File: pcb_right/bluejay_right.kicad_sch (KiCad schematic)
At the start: 69 parts, among them J2 SJ-43514, U2 MCP23017

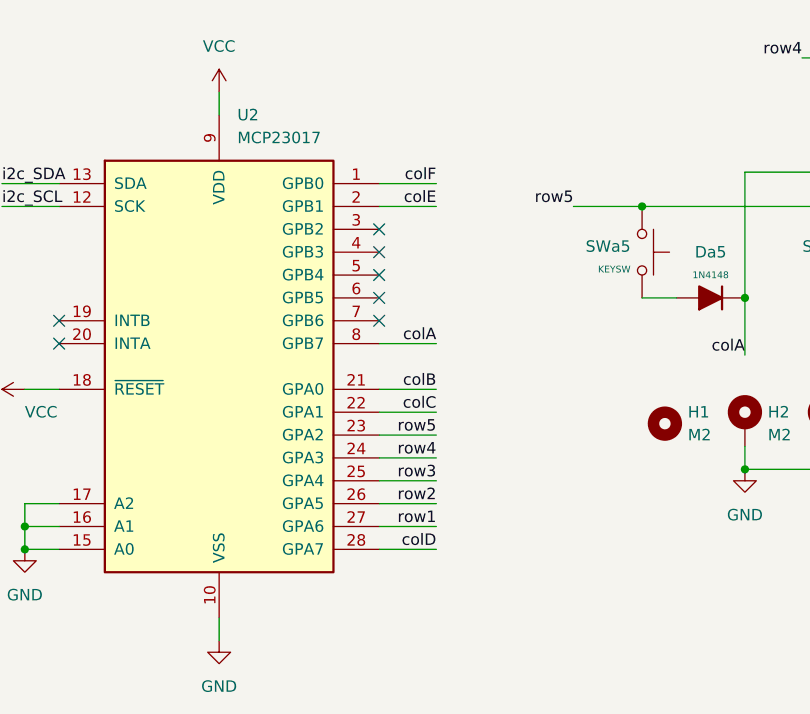
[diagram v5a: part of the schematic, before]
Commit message: Create base pcb
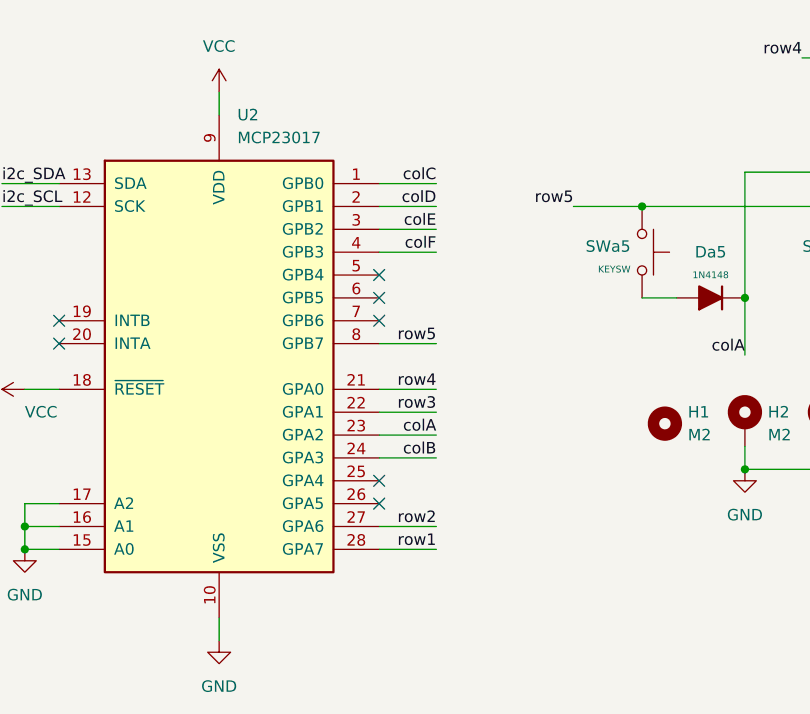
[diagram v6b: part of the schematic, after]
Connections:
- net colA: now also U2.23 (GPA2); no longer U2.8 (GPB7)
- net colB: now also U2.24 (GPA3); no longer U2.21 (GPA0)
- net colC: now also U2.1 (GPB0); no longer U2.22 (GPA1)
- net colD: now also U2.2 (GPB1); no longer U2.28 (GPA7)
- net colE: now also U2.3 (GPB2); no longer U2.2 (GPB1)
- net colF: now also U2.4 (GPB3); no longer U2.1 (GPB0)
- net row1: now also U2.28 (GPA7); no longer U2.27 (GPA6)
- net row2: now also U2.27 (GPA6); no longer U2.26 (GPA5)
- net row3: now also U2.22 (GPA1); no longer U2.25 (GPA4)
- net row4: now also U2.21 (GPA0); no longer U2.24 (GPA3)
- net row5: now also U2.8 (GPB7); no longer U2.23 (GPA2)
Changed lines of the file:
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@@
   (junction (at 104.14 120.65) (diameter 0) (color 0 0 0 0)
   )
-  (no_connect (at 63.5 101.6))
-  (no_connect (at 63.5 96.52))
   (no_connect (at 63.5 99.06))
   (no_connect (at 63.5 104.14))
-  (no_connect (at 63.5 93.98))
+  (no_connect (at 63.5 101.6))
   (no_connect (at 27.94 104.14))
   (no_connect (at 27.94 106.68))
+  (no_connect (at 63.5 124.46))
+  (no_connect (at 63.5 121.92))
   (wire (pts (xy 55.88 49.53) (xy 55.88 52.07))
     (stroke (width 0) (type default) (color 0 0 0 0))
   )
+  (wire (pts (xy 48.26 49.53) (xy 48.26 59.69))
+    (stroke (width 0) (type default) (color 0 0 0 0))
+  )
+  (wire (pts (xy 222.25 59.69) (xy 218.44 59.69))
+    (stroke (width 0) (type default) (color 0 0 0 0))
+  )
+  (wire (pts (xy 133.35 59.69) (xy 133.35 72.39))
+    (stroke (width 0) (type default) (color 0 0 0 0))
+  )
+  (wire (pts (xy 194.31 36.83) (xy 170.18 36.83))
+    (stroke (width 0) (type default) (color 0 0 0 0))
+  )
+  (wire (pts (xy 246.38 72.39) (xy 242.57 72.39))
+    (stroke (width 0) (type default) (color 0 0 0 0))
+  )
+  (wire (pts (xy 63.5 119.38) (xy 69.85 119.38))
+    (stroke (width 0) (type default) (color 0 0 0 0))
+  )
+  (wire (pts (xy 48.26 59.69) (xy 58.42 59.69))
+    (stroke (width 0) (type default) (color 0 0 0 0))
+  )
+  (wire (pts (xy 246.38 85.09) (xy 242.57 85.09))
+    (stroke (width 0) (type default) (color 0 0 0 0))
+  )
+  (wire (pts (xy 181.61 85.09) (xy 181.61 90.17))
+    (stroke (width 0) (type default) (color 0 0 0 0))
+  )
+  (wire (pts (xy 219.71 104.14) (xy 219.71 105.41))
+    (stroke (width 0) (type default) (color 0 0 0 0))
+  )
+  (wire (pts (xy 113.03 118.11) (xy 113.03 120.65))
+    (stroke (width 0) (type default) (color 0 0 0 0))
+  )
+  (wire (pts (xy 152.4 90.17) (xy 152.4 101.6))
+    (stroke (width 0) (type default) (color 0 0 0 0))
+  )
+  (wire (pts (xy 104.14 87.63) (xy 104.14 101.6))
+    (stroke (width 0) (type default) (color 0 0 0 0))
+  )
+  (wire (pts (xy 48.26 40.64) (xy 48.26 44.45))
+    (stroke (width 0) (type default) (color 0 0 0 0))
+  )
+  (wire (pts (xy 246.38 59.69) (xy 242.57 59.69))
+    (stroke (width 0) (type default) (color 0 0 0 0))
+  )
+  (wire (pts (xy 198.12 59.69) (xy 194.31 59.69))
+    (stroke (width 0) (type default) (color 0 0 0 0))
+  )
+  (wire (pts (xy 121.92 49.53) (xy 110.49 49.53))
+    (stroke (width 0) (type default) (color 0 0 0 0))
+  )
+  (wire (pts (xy 194.31 74.93) (xy 170.18 74.93))
+    (stroke (width 0) (type default) (color 0 0 0 0))
+  )
+  (wire (pts (xy 38.1 52.07) (xy 55.88 52.07))
+    (stroke (width 0) (type default) (color 0 0 0 0))
+  )
+  (wire (pts (xy 173.99 46.99) (xy 170.18 46.99))
+    (stroke (width 0) (type default) (color 0 0 0 0))
+  )
+  (wire (pts (xy 125.73 85.09) (xy 121.92 85.09))
+    (stroke (width 0) (type default) (color 0 0 0 0))
+  )
+  (wire (pts (xy 21.59 88.9) (xy 27.94 88.9))
+    (stroke (width 0) (type default) (color 0 0 0 0))
+  )
+  (wire (pts (xy 205.74 72.39) (xy 205.74 85.09))
+    (stroke (width 0) (type default) (color 0 0 0 0))
+  )
   (wire (pts (xy 63.5 116.84) (xy 69.85 116.84))
     (stroke (width 0) (type default) (color 0 0 0 0))
   )
-  (wire (pts (xy 48.26 49.53) (xy 48.26 59.69))
-    (stroke (width 0) (type default) (color 0 0 0 0))
-  )
-  (wire (pts (xy 222.25 59.69) (xy 218.44 59.69))
-    (stroke (width 0) (type default) (color 0 0 0 0))
-  )
-  (wire (pts (xy 133.35 59.69) (xy 133.35 72.39))
-    (stroke (width 0) (type default) (color 0 0 0 0))
-  )
-  (wire (pts (xy 194.31 36.83) (xy 170.18 36.83))
-    (stroke (width 0) (type default) (color 0 0 0 0))
-  )
-  (wire (pts (xy 63.5 121.92) (xy 69.85 121.92))
-    (stroke (width 0) (type default) (color 0 0 0 0))
-  )
-  (wire (pts (xy 246.38 72.39) (xy 242.57 72.39))
-    (stroke (width 0) (type default) (color 0 0 0 0))
-  )
-  (wire (pts (xy 48.26 59.69) (xy 58.42 59.69))
-    (stroke (width 0) (type default) (color 0 0 0 0))
-  )
-  (wire (pts (xy 246.38 85.09) (xy 242.57 85.09))
-    (stroke (width 0) (type default) (color 0 0 0 0))
-  )
-  (wire (pts (xy 181.61 85.09) (xy 181.61 90.17))
-    (stroke (width 0) (type default) (color 0 0 0 0))
-  )
-  (wire (pts (xy 219.71 104.14) (xy 219.71 105.41))
-    (stroke (width 0) (type default) (color 0 0 0 0))
-  )
-  (wire (pts (xy 113.03 118.11) (xy 113.03 120.65))
-    (stroke (width 0) (type default) (color 0 0 0 0))
-  )
-  (wire (pts (xy 152.4 90.17) (xy 152.4 101.6))
-    (stroke (width 0) (type default) (color 0 0 0 0))
-  )
-  (wire (pts (xy 104.14 87.63) (xy 104.14 101.6))
-    (stroke (width 0) (type default) (color 0 0 0 0))
-  )
-  (wire (pts (xy 48.26 40.64) (xy 48.26 44.45))
-    (stroke (width 0) (type default) (color 0 0 0 0))
-  )
-  (wire (pts (xy 246.38 59.69) (xy 242.57 59.69))
-    (stroke (width 0) (type default) (color 0 0 0 0))
-  )
-  (wire (pts (xy 198.12 59.69) (xy 194.31 59.69))
-    (stroke (width 0) (type default) (color 0 0 0 0))
-  )
-  (wire (pts (xy 121.92 49.53) (xy 110.49 49.53))
-    (stroke (width 0) (type default) (color 0 0 0 0))
-  )
-  (wire (pts (xy 194.31 74.93) (xy 170.18 74.93))
-    (stroke (width 0) (type default) (color 0 0 0 0))
-  )
-  (wire (pts (xy 38.1 52.07) (xy 55.88 52.07))
-    (stroke (width 0) (type default) (color 0 0 0 0))
-  )
-  (wire (pts (xy 173.99 46.99) (xy 170.18 46.99))
-    (stroke (width 0) (type default) (color 0 0 0 0))
-  )
-  (wire (pts (xy 125.73 85.09) (xy 121.92 85.09))
-    (stroke (width 0) (type default) (color 0 0 0 0))
-  )
-  (wire (pts (xy 21.59 88.9) (xy 27.94 88.9))
-    (stroke (width 0) (type default) (color 0 0 0 0))
-  )
-  (wire (pts (xy 205.74 72.39) (xy 205.74 85.09))
-    (stroke (width 0) (type default) (color 0 0 0 0))
-  )
   (wire (pts (xy 21.59 91.44) (xy 27.94 91.44))
     (stroke (width 0) (type default) (color 0 0 0 0))
@@
     (stroke (width 0) (type default) (color 0 0 0 0))
   )
-  (wire (pts (xy 63.5 119.38) (xy 69.85 119.38))
-    (stroke (width 0) (type default) (color 0 0 0 0))
-  )
   (wire (pts (xy 133.35 72.39) (xy 133.35 85.09))
     (stroke (width 0) (type default) (color 0 0 0 0))
@@
     (stroke (width 0) (type default) (color 0 0 0 0))
   )
-  (wire (pts (xy 63.5 124.46) (xy 69.85 124.46))
-    (stroke (width 0) (type default) (color 0 0 0 0))
-  )
   (wire (pts (xy 152.4 101.6) (xy 152.4 107.95))
     (stroke (width 0) (type default) (color 0 0 0 0))
@@
     (stroke (width 0) (type default) (color 0 0 0 0))
   )
+  (wire (pts (xy 63.5 93.98) (xy 69.85 93.98))
+    (stroke (width 0) (type default) (color 0 0 0 0))
+  )
   (wire (pts (xy 229.87 104.14) (xy 219.71 104.14))
     (stroke (width 0) (type default) (color 0 0 0 0))
@@
   )
   (wire (pts (xy 144.78 101.6) (xy 140.97 101.6))
+    (stroke (width 0) (type default) (color 0 0 0 0))
+  )
+  (wire (pts (xy 63.5 96.52) (xy 69.85 96.52))
     (stroke (width 0) (type default) (color 0 0 0 0))
   )
@@
     (effects (font (size 1.27 1.27)) (justify left bottom))
   )
-  (label "colF" (at 69.85 88.9 180)
+  (label "colF" (at 69.85 96.52 180)
     (effects (font (size 1.27 1.27)) (justify right bottom))
   )
@@
     (effects (font (size 1.27 1.27)) (justify right bottom))
   )
-  (label "colE" (at 69.85 91.44 180)
-    (effects (font (size 1.27 1.27)) (justify right bottom))
-  )
-  (label "colC" (at 69.85 114.3 180)
-    (effects (font (size 1.27 1.27)) (justify right bottom))
-  )
-  (label "row2" (at 69.85 124.46 180)
-    (effects (font (size 1.27 1.27)) (justify right bottom))
-  )
-  (label "colB" (at 69.85 111.76 180)
+  (label "colE" (at 69.85 93.98 180)
+    (effects (font (size 1.27 1.27)) (justify right bottom))
+  )
+  (label "colC" (at 69.85 88.9 180)
+    (effects (font (size 1.27 1.27)) (justify right bottom))
+  )
+  (label "row2" (at 69.85 127 180)
+    (effects (font (size 1.27 1.27)) (justify right bottom))
+  )
+  (label "colB" (at 69.85 119.38 180)
     (effects (font (size 1.27 1.27)) (justify right bottom))
   )
@@
     (effects (font (size 1.27 1.27)) (justify right bottom))
   )
-  (label "row4" (at 69.85 119.38 180)
-    (effects (font (size 1.27 1.27)) (justify right bottom))
-  )
-  (label "colA" (at 69.85 106.68 180)
+  (label "row4" (at 69.85 111.76 180)
+    (effects (font (size 1.27 1.27)) (justify right bottom))
+  )
+  (label "colA" (at 69.85 116.84 180)
     (effects (font (size 1.27 1.27)) (justify right bottom))
   )
@@
     (effects (font (size 1.27 1.27)) (justify left bottom))
   )
-  (label "colD" (at 69.85 129.54 180)
-    (effects (font (size 1.27 1.27)) (justify right bottom))
-  )
-  (label "row5" (at 69.85 116.84 180)
+  (label "colD" (at 69.85 91.44 180)
+    (effects (font (size 1.27 1.27)) (justify right bottom))
+  )
+  (label "row5" (at 69.85 106.68 180)
     (effects (font (size 1.27 1.27)) (justify right bottom))
   )
@@
     (effects (font (size 1.27 1.27)) (justify right bottom))
   )
-  (label "row3" (at 69.85 121.92 180)
+  (label "row3" (at 69.85 114.3 180)
     (effects (font (size 1.27 1.27)) (justify right bottom))
   )
@@
     (effects (font (size 1.27 1.27)) (justify right bottom))
   )
-  (label "row1" (at 69.85 127 180)
-    (effects (font (size 1.27 1.27)) (justify right bottom))
-  )
+  (label "row1" (at 69.85 129.54 180)
+    (effects (font (size 1.27 1.27)) (justify right bottom))
+  )

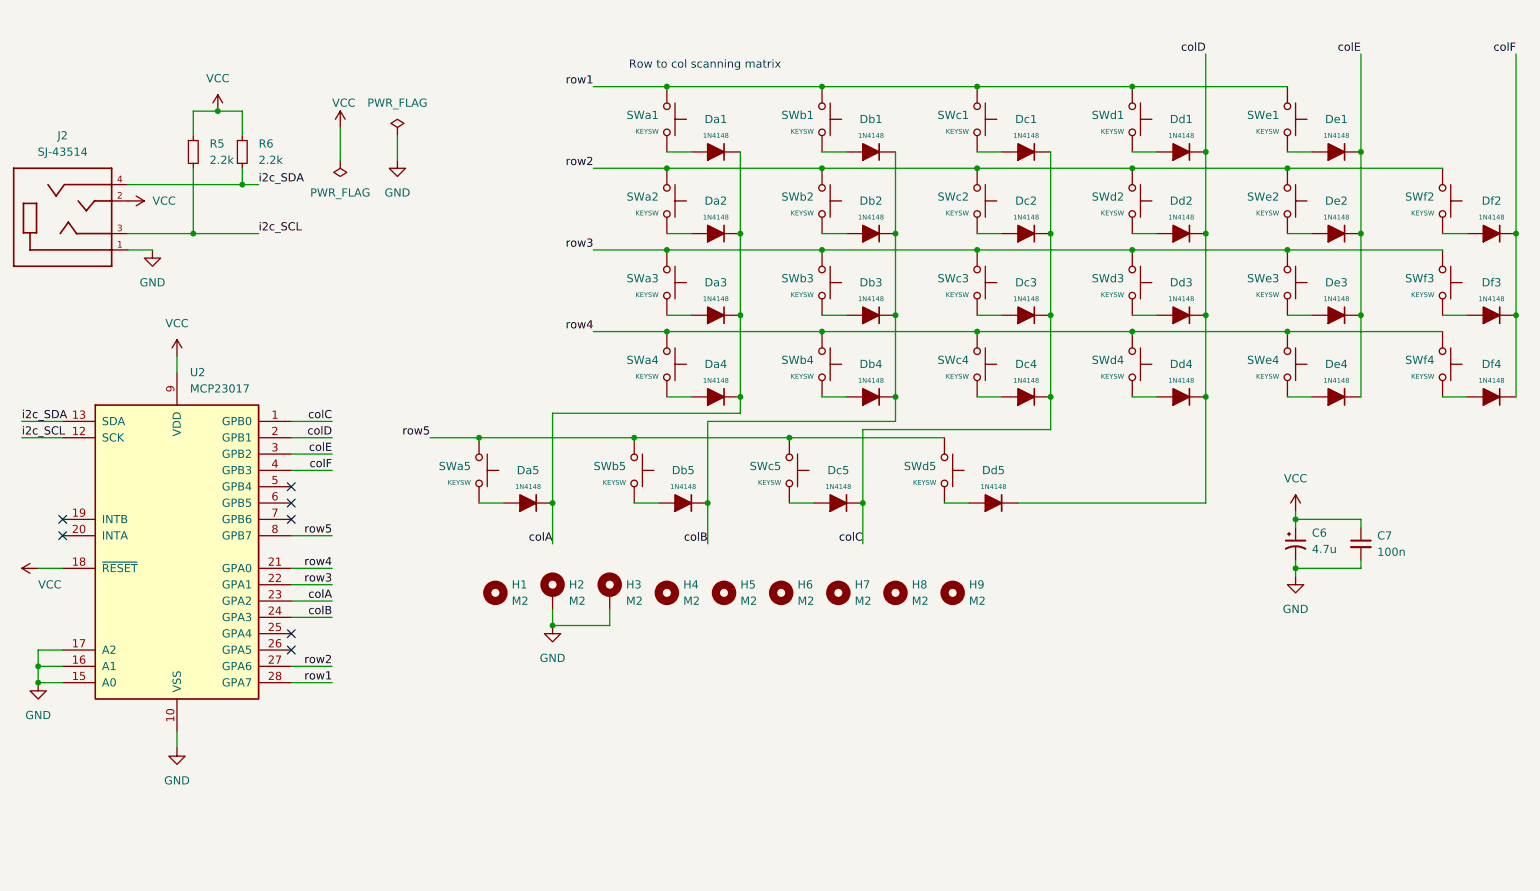
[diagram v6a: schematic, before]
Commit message: Update schematics in preparation for review
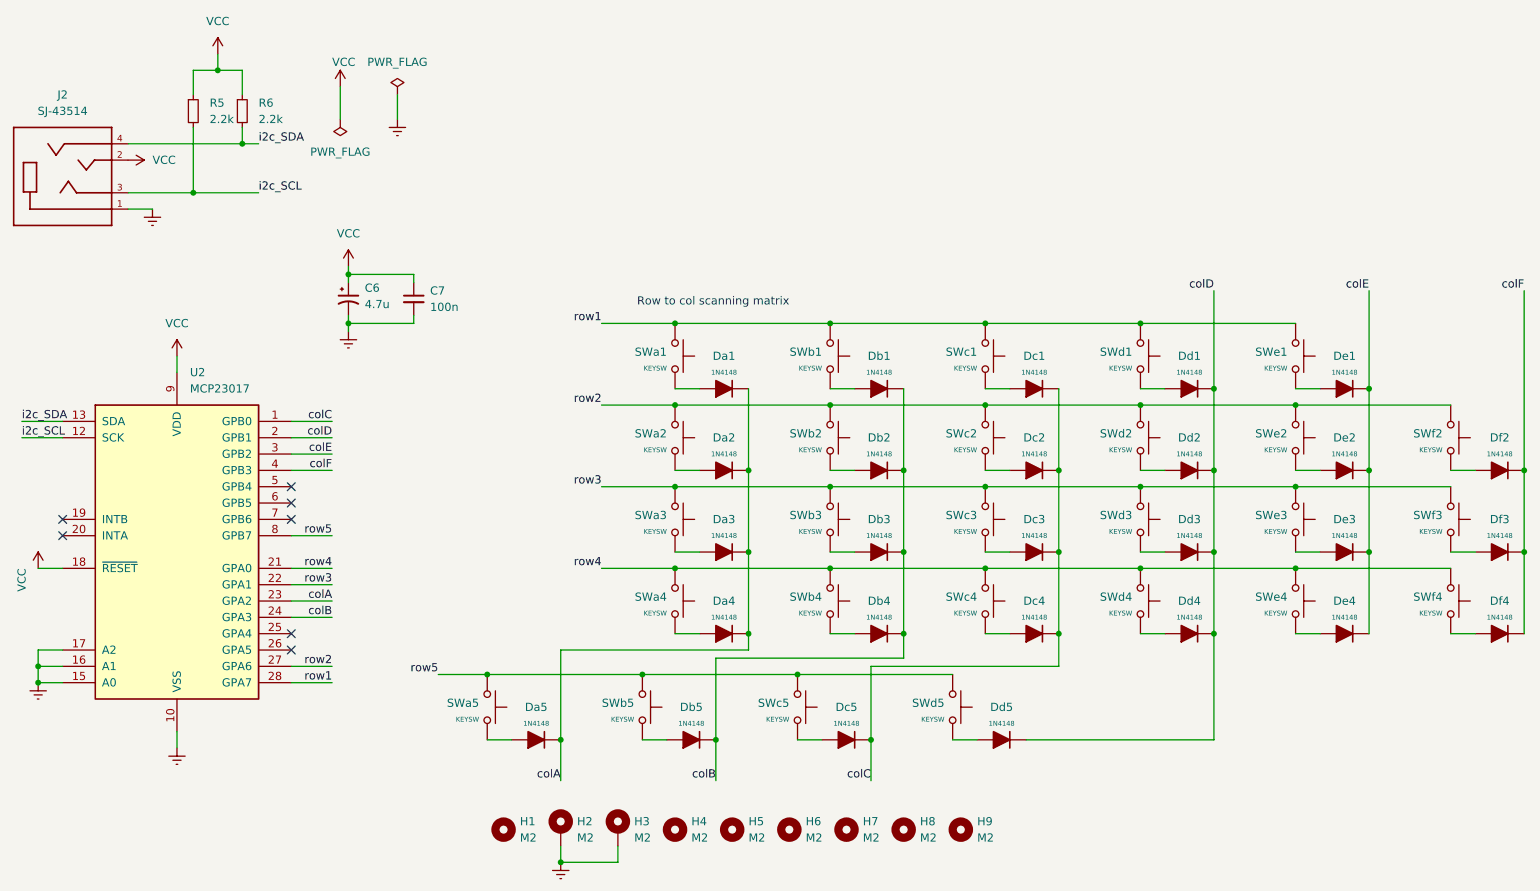
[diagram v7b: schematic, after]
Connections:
- net GND renamed Earth
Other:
- moved on the sheet: C6, C7, Da1, Da2, Da3, Da4, Da5, Db1, Db2, Db3, Db4, Db5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

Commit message: Fine tuning of schematics and pcbs in prep for review
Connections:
- net Earth renamed GND
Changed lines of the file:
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@@
     (pin "2")
   )
-  (symbol (lib_id "power:Earth") (at 80.01 41.91 0) (unit 1)
+  (symbol (lib_id "power:GND") (at 80.01 41.91 0) (unit 1)
     (in_bom yes) (on_board yes) (fields_autoplaced)
     (property "Reference" "#PWR0108" (id 0) (at 80.01 48.26 0)
       (effects (font (size 1.27 1.27)) hide)
     )
-    (property "Value" "Earth" (id 1) (at 80.01 45.72 0)
-      (effects (font (size 1.27 1.27)) hide)
-    )
+    (property "Value" "GND" (id 1) (at 80.01 45.72 0))
     (property "Footprint" "" (id 2) (at 80.01 41.91 0)
       (effects (font (size 1.27 1.27)) hide)
@@
     (pin "1")
   )
-  (symbol (lib_id "power:Earth") (at 45.72 139.7 0) (unit 1)
+  (symbol (lib_id "power:GND") (at 45.72 139.7 0) (unit 1)
     (in_bom yes) (on_board yes) (fields_autoplaced)
     (property "Reference" "#PWR0104" (id 0) (at 45.72 146.05 0)
       (effects (font (size 1.27 1.27)) hide)
     )
-    (property "Value" "Earth" (id 1) (at 45.72 143.51 0)
+    (property "Value" "GND" (id 1) (at 45.72 143.51 0)
       (effects (font (size 1.27 1.27)) hide)
     )
@@
     (pin "2")
   )
-  (symbol (lib_id "power:Earth") (at 72.39 74.93 0) (unit 1)
+  (symbol (lib_id "power:GND") (at 72.39 74.93 0) (unit 1)
     (in_bom yes) (on_board yes) (fields_autoplaced)
     (property "Reference" "#PWR0102" (id 0) (at 72.39 81.28 0)
       (effects (font (size 1.27 1.27)) hide)
     )
-    (property "Value" "Earth" (id 1) (at 72.39 78.74 0)
+    (property "Value" "GND" (id 1) (at 72.39 78.74 0)
       (effects (font (size 1.27 1.27)) hide)
     )
@@
     (pin "2")
   )
-  (symbol (lib_id "power:Earth") (at 105.41 157.48 0) (unit 1)
+  (symbol (lib_id "power:GND") (at 105.41 157.48 0) (unit 1)
     (in_bom yes) (on_board yes) (fields_autoplaced)
     (property "Reference" "#PWR0110" (id 0) (at 105.41 163.83 0)
       (effects (font (size 1.27 1.27)) hide)
     )
-    (property "Value" "Earth" (id 1) (at 105.41 161.29 0)
+    (property "Value" "GND" (id 1) (at 105.41 161.29 0)
       (effects (font (size 1.27 1.27)) hide)
     )
@@
     (pin "1")
   )
-  (symbol (lib_id "power:Earth") (at 41.91 55.88 0) (unit 1)
+  (symbol (lib_id "power:GND") (at 41.91 55.88 0) (unit 1)
     (in_bom yes) (on_board yes) (fields_autoplaced)
     (property "Reference" "#PWR0113" (id 0) (at 41.91 62.23 0)
       (effects (font (size 1.27 1.27)) hide)
     )
-    (property "Value" "Earth" (id 1) (at 41.91 59.69 0)
-      (effects (font (size 1.27 1.27)) hide)
-    )
+    (property "Value" "GND" (id 1) (at 41.91 59.69 0))
     (property "Footprint" "" (id 2) (at 41.91 55.88 0)
       (effects (font (size 1.27 1.27)) hide)
@@
     (pin "1")
   )
-  (symbol (lib_id "power:Earth") (at 24.13 129.54 0) (unit 1)
+  (symbol (lib_id "power:GND") (at 24.13 129.54 0) (unit 1)
     (in_bom yes) (on_board yes) (fields_autoplaced)
     (property "Reference" "#PWR0105" (id 0) (at 24.13 135.89 0)
       (effects (font (size 1.27 1.27)) hide)
     )
-    (property "Value" "Earth" (id 1) (at 24.13 133.35 0)
+    (property "Value" "GND" (id 1) (at 24.13 133.35 0)
       (effects (font (size 1.27 1.27)) hide)
     )
@@
     )
     (path "/4a764b71-3549-41f2-956b-5e0c88d08a53"
-      (reference "#PWR0102") (unit 1) (value "Earth") (footprint "")
+      (reference "#PWR0102") (unit 1) (value "GND") (footprint "")
     )
     (path "/dfb0ebe7-94a3-42d3-9cea-62101ad66267"
@@
     )
     (path "/2e56cb98-1e69-4e72-a6ae-a689c82ca83d"
-      (reference "#PWR0104") (unit 1) (value "Earth") (footprint "")
+      (reference "#PWR0104") (unit 1) (value "GND") (footprint "")
     )
     (path "/e056007b-7feb-409f-81eb-ea1fa58de922"
-      (reference "#PWR0105") (unit 1) (value "Earth") (footprint "")
+      (reference "#PWR0105") (unit 1) (value "GND") (footprint "")
     )
     (path "/b3fae681-c665-44b6-9402-e730b55c6c60"
@@
     )
     (path "/2618b08a-8c24-4bae-8ac0-cea4e2a72337"
-      (reference "#PWR0108") (unit 1) (value "Earth") (footprint "")
+      (reference "#PWR0108") (unit 1) (value "GND") (footprint "")
     )
     (path "/8af62b85-70d4-408c-8ccc-24c5f9793b2a"
@@
     )
     (path "/5c628fb1-db6b-4a2b-bba3-1f81260cfadb"
-      (reference "#PWR0110") (unit 1) (value "Earth") (footprint "")
+      (reference "#PWR0110") (unit 1) (value "GND") (footprint "")
     )
     (path "/248864a2-91ef-4d14-87e7-7b68a9c3eb73"
@@
     )
     (path "/5db823f5-1028-4c25-9628-3c5bc8f81679"
-      (reference "#PWR0113") (unit 1) (value "Earth") (footprint "")
+      (reference "#PWR0113") (unit 1) (value "GND") (footprint "")
     )
     (path "/25d4dae8-ca7e-4cc9-b35f-a678ed89288b"
